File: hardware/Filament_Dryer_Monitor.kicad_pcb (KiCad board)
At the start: 4 copper layers, 95 x 52 mm, 94 parts, among them J1 DC Connector, J2 USB_C_Receptacle_USB2.0_16P, J3 Sensor, J4 Display, J5 Heater Connector, J6 Fan Connector, J7 NTC Connector, Q1 DMP6180SK3-13, Q2 MMBT3904, Q3 MMBT3904, Q4 NTD5865NLT4G, Q5 CJ2310, Q6 MMBT3904, SW1 SW_RST, SW2 SW_BOOT, SW3 On/Off, SW4 Mode, SW5 Up, SW6 Down, U1 AP66200, U2 CP2102N-A02-GQFN28, U3 USBLC6-2SC6, U4 ESP32-WROOM-32E-N4

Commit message: Complete PCB layout: first release-ready hardware revision
Finalize board layout, add J3 sensor connector to BOM/position files,
and fix switch label properties (Value/Function swapped for SW1-6).
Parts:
- added REF**: Slewform_Logo_20mm, Slewform:Slewform_Logo_20mm, B.Cu at (149.0, 94.5)
- SW1: value SW_RST -> ~
- SW2: value SW_BOOT -> ~
- SW3: value On/Off -> ~
- SW4: value Mode -> ~
- SW5: value Up -> ~
- SW6: value Down -> ~
- U2: value CP2102N-A02-GQFN28 -> CP2102N-A02-GQFN28R
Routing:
- net /MCU/ESP_RXD0: track 38.6 -> 39.1 mm

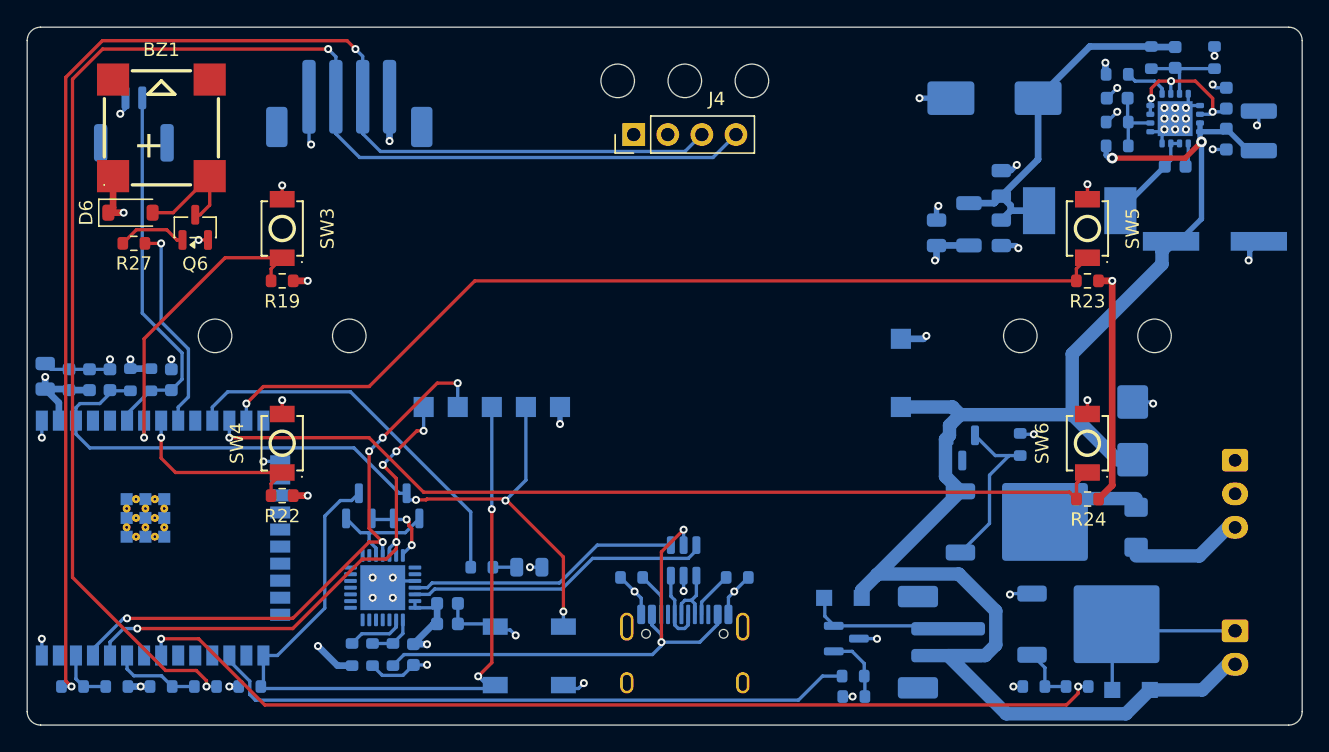
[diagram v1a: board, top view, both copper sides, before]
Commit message: Add HEATER_SW net label and tighten via design rules
Rename Power_Heat netclass pattern to match the new HEATER_SW label,
reduce min via annular width/diameter, and update PCB layout
accordingly. Add STL export of the board.
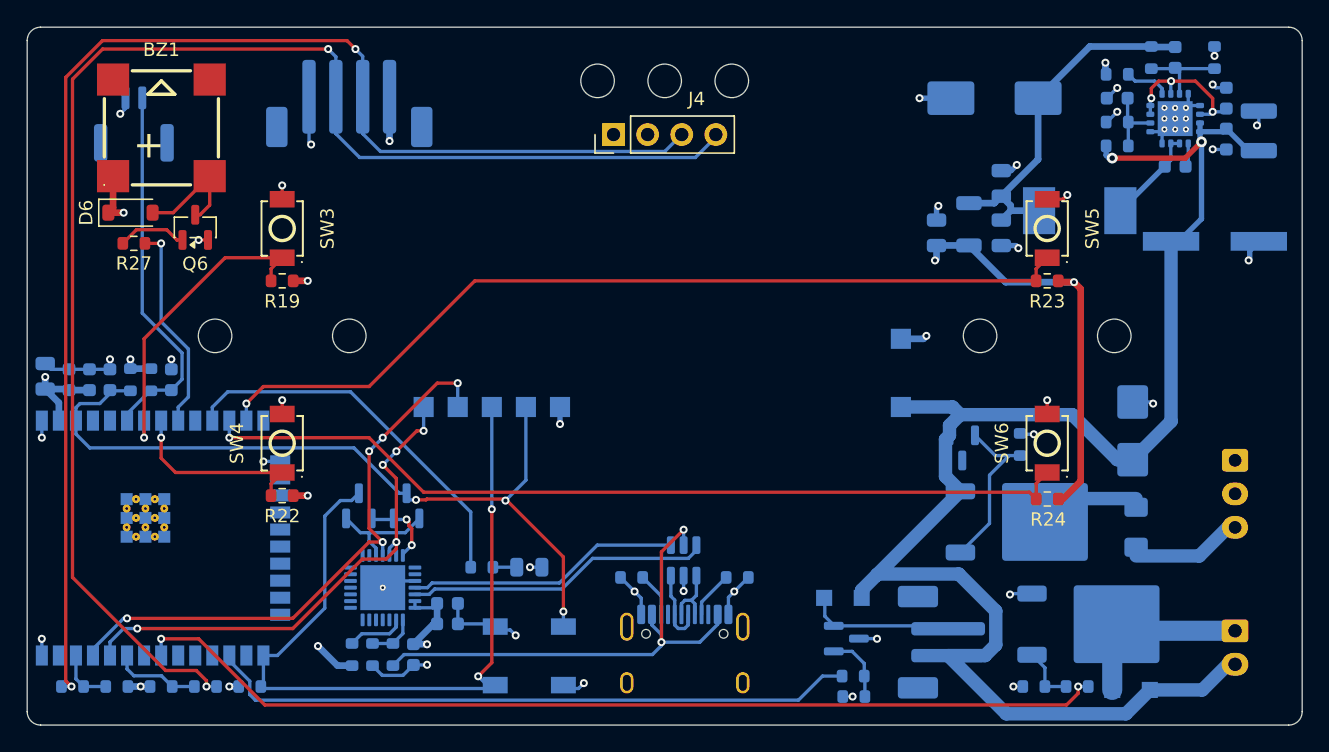
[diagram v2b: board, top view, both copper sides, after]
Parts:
- moved R23 3.00 mm to (176.0, 98.9)
- moved R24 3.00 mm to (176.0, 115.2)
- moved REF** 3.00 mm to (181.0, 103.0)
- moved REF** 3.00 mm to (171.0, 103.0)
- moved SW5 3.00 mm to (176.0, 95.0)
- moved SW6 3.00 mm to (176.0, 111.0)
- moved ? 1.50 mm to (147.5, 84.0)
- moved ? 1.50 mm to (152.5, 84.0)
- moved ? 1.50 mm to (142.5, 84.0)
- moved J4 1.50 mm to (143.7, 88.0)
- moved REF** 1.50 mm to (147.5, 94.5)
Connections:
- net Net-(D4-A) renamed /IO_Power/HEATER_SW
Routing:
- net 3V3_MCU: track 55.5 -> 65.3 mm
- net BTN_UP: track 69.0 -> 66.0 mm
- net BTN_DOWN: track 68.6 -> 65.6 mm
- net Net-(J3-Pin_3): track 102.2 -> 100.7 mm
- net 24V_PROT: track 117.3 -> 118.7 mm
- net Net-(J3-Pin_2): track 109.3 -> 107.9 mm
- net GND: track 69.5 -> 70.1 mm, vias 50 -> 47
